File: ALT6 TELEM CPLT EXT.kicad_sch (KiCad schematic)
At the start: 22 parts, among them IC1 USBLC6-2SC6, IC2 USBLC6-2SC6, IC3 USBLC6-2SC6, J1 2200301031, J2 2200301031, J3 2200301021, J4 SSQ-120-01-L-D, J5 2200301031

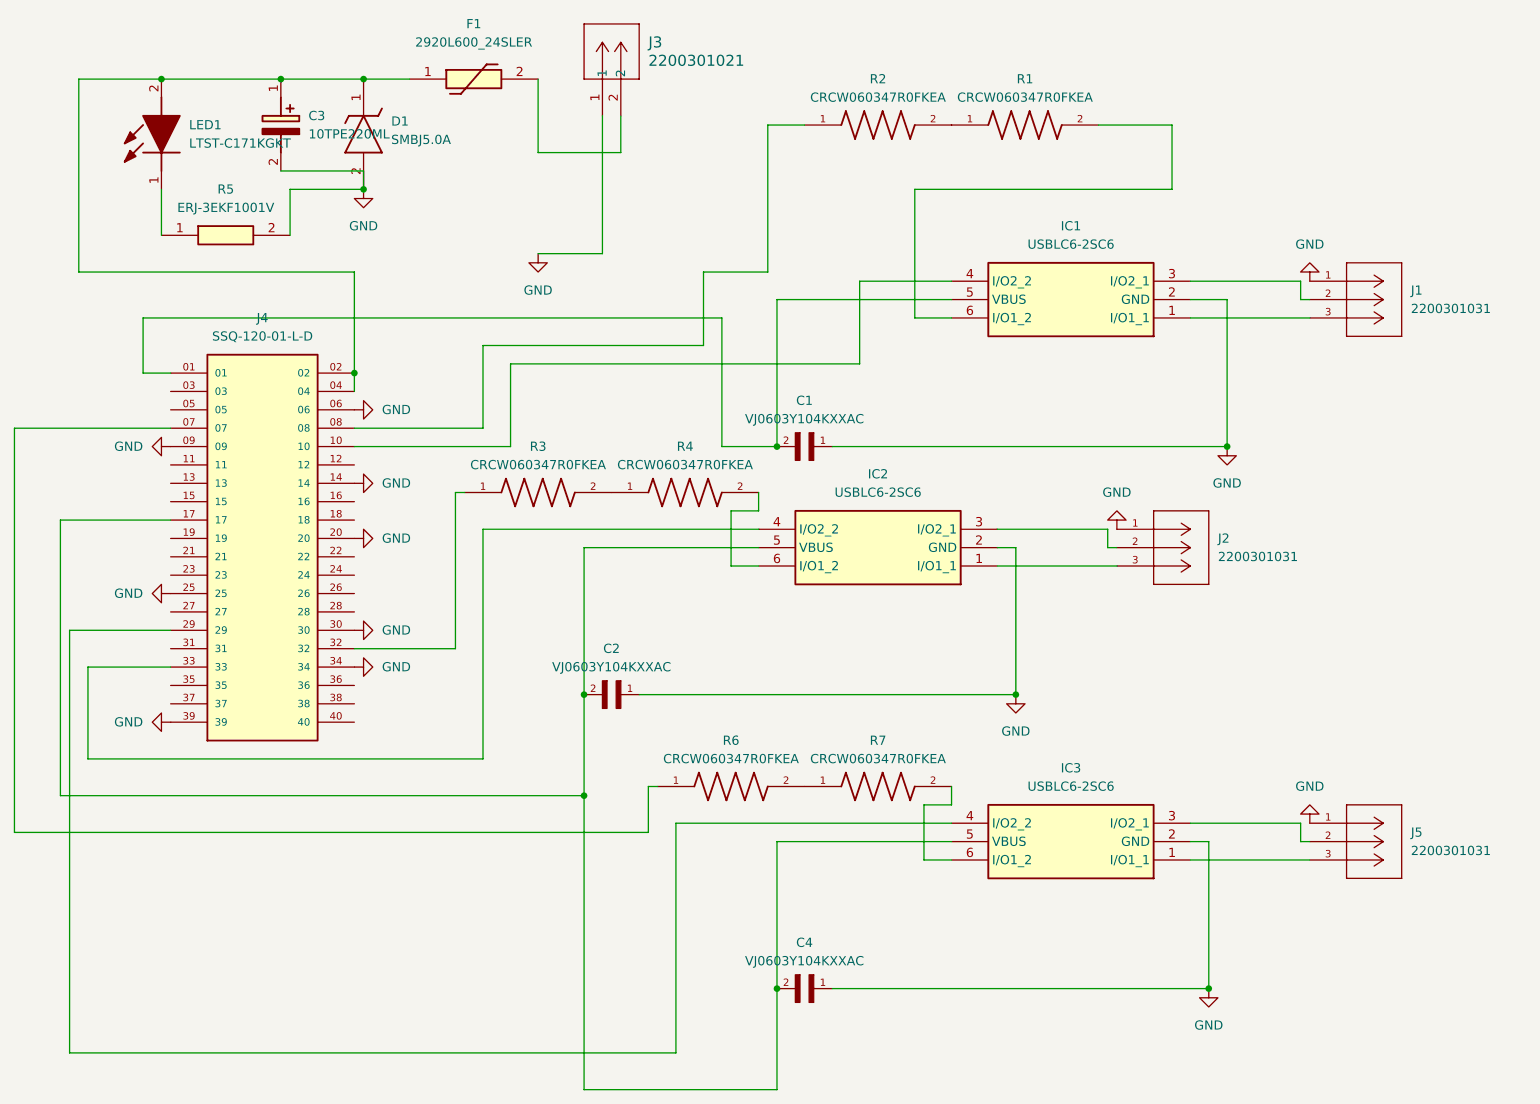
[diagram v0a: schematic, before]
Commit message: Connectors change
Connectors change to vertical, improve trace design, add 0ohm in RX line to test, change the power connector (was very big and innecesary)
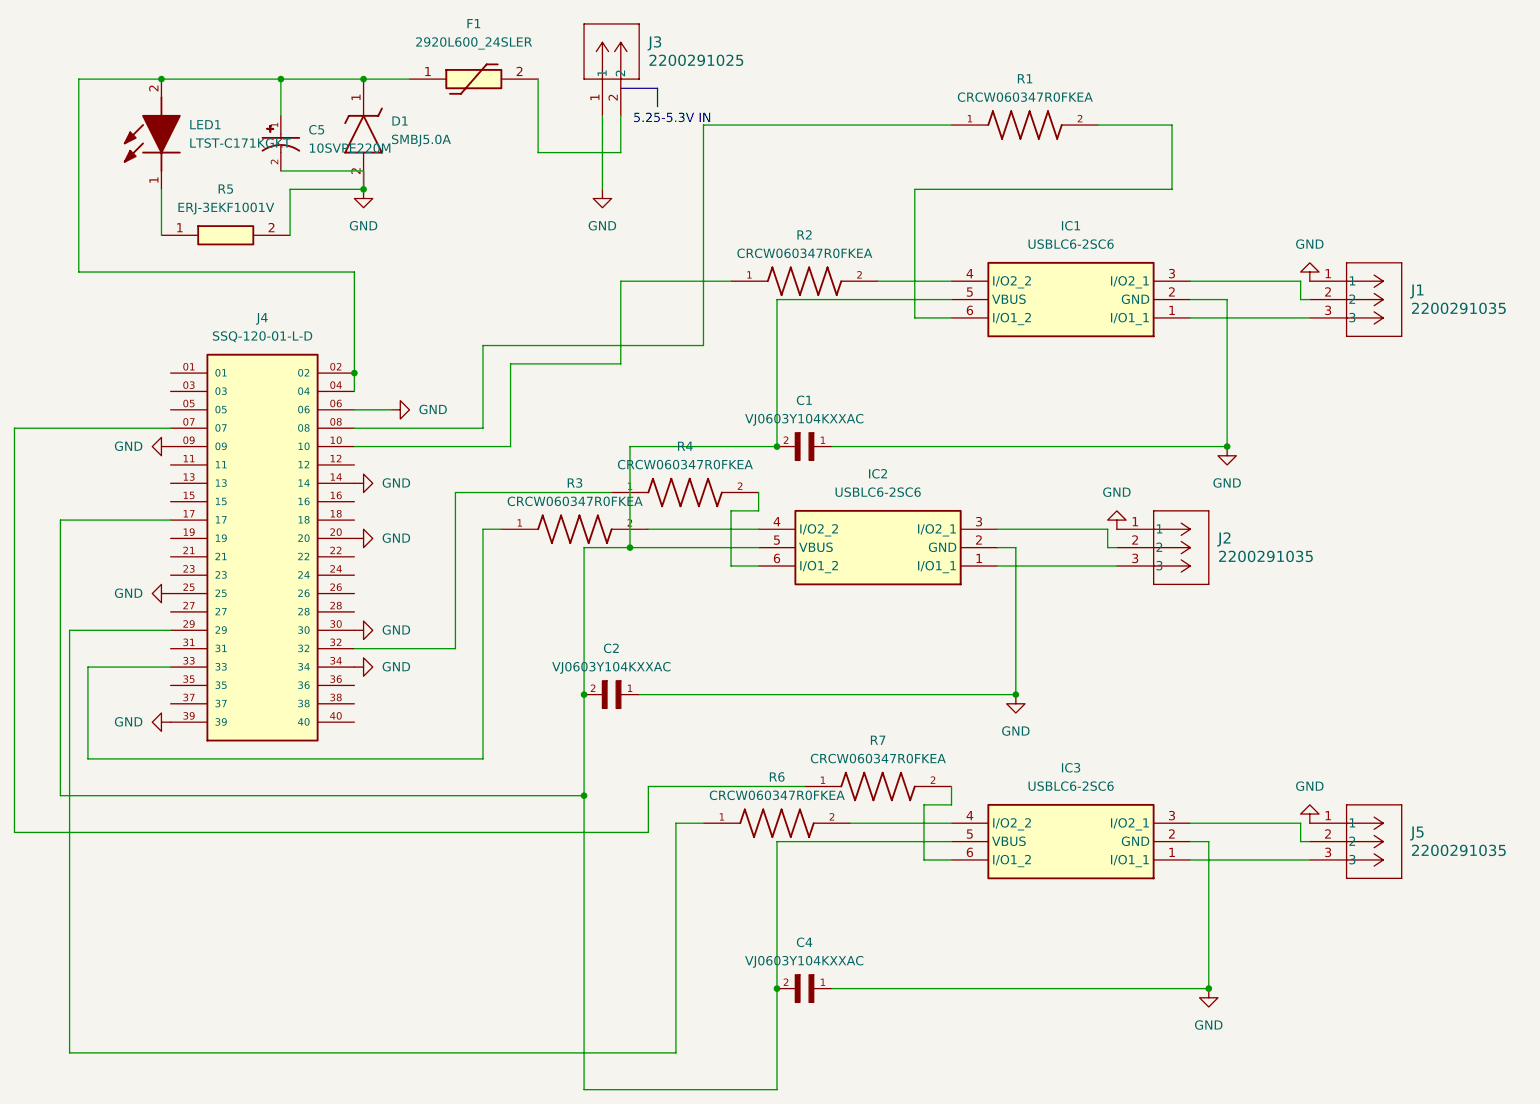
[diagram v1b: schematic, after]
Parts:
- removed C3: 10TPE220ML, 16TDC150MYF, symbol 10TPE220ML:10TPE220ML
- removed J1, J2, J5: 2200301031, 2200301031:CONN_2200300000-SD_03_MOL, symbol 2200301031:2200301031
- removed J3: 2200301021, CONN_2200300000-SD_02_MOL, symbol 2200301021:2200301021
- added C5: 10SVPE220M, 10SVPE220M:CAP_10SVPE220M, symbol 10SVPE220M:10SVPE220M
- added J1, J2, J5: 2200291035, CONN_2200290000-SD_03_MOL, symbol 2200291035:2200291035
- added J3: 2200291025, CONN_2200290000-SD_02_MOL, symbol 2200291025:2200291025
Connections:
- net GND: now also C5.2, J1.1, J2.1, J3.1, J5.1
- net at F1.2: now also J3.2
- net at C1.2, IC1.5 (VBUS): now also C2.2, C4.2, IC2.5 (VBUS), IC3.5 (VBUS), J4.17; no longer J4.01
- net at D1.1 (K), F1.1, J4.02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: now also C5.1
- net at J4.07: now also R7.1; no longer R6.1
- net at J4.08: now also R1.1; no longer R2.1
- net at J4.10: now also R2.1; no longer IC1.4 (I/O2_2)
- net at J4.29: now also R6.1; no longer IC3.4 (I/O2_2)
- net at J4.32: now also R4.1; no longer R3.1
- net at J4.33: now also R3.1; no longer IC2.4 (I/O2_2)
- net at R2.2: now also IC1.4 (I/O2_2); no longer R1.1
- net at IC3.1 (I/O1_1): now also J5.3
- net at IC3.3 (I/O2_1): now also J5.2
- net at R3.2: now also IC2.4 (I/O2_2); no longer R4.1
- net at IC1.1 (I/O1_1): now also J1.3
- net at IC1.3 (I/O2_1): now also J1.2
- net at R6.2: now also IC3.4 (I/O2_2); no longer R7.1
- net at IC2.3 (I/O2_1): now also J2.2
- net at IC2.1 (I/O1_1): now also J2.3
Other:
- note added: "5.25-5.3V IN"

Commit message: Complete Schematic
added labels in the schematic
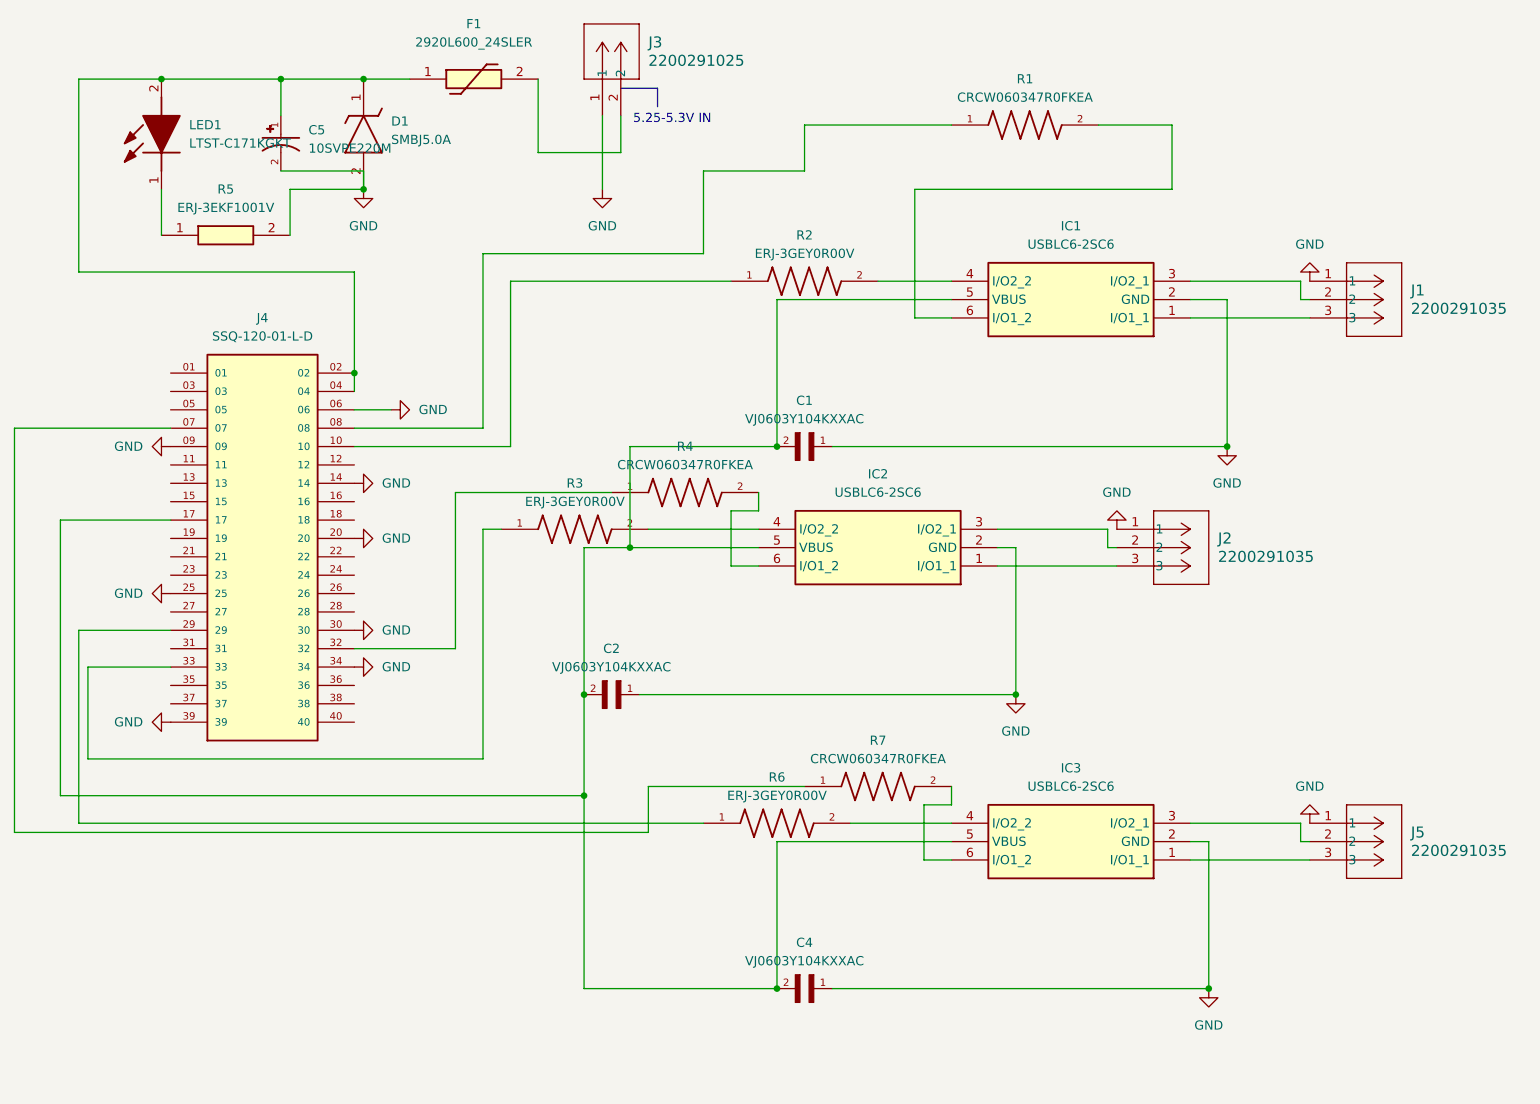
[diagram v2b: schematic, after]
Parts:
- removed R2, R3, R6: CRCW060347R0FKEA, CRCW060347R0FKEA:RESC1508X50N, symbol CRCW060347R0FKEA:CRCW060347R0FKEA
- added R2, R3, R6: ERJ-3GEY0R00V, ERJ-3GEY0R00V:RES_ERJ-3GEY0R00V, symbol ERJ-3GEY0R00V:ERJ-3GEY0R00V
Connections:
- net at J4.10: now also R2.1
- net at J4.29: now also R6.1
- net at J4.33: now also R3.1
- net at IC2.4 (I/O2_2): now also R3.2
- net at IC3.4 (I/O2_2): now also R6.2
- net at IC1.4 (I/O2_2): now also R2.2

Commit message: Reupload footprints
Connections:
- no-connect marks 0 -> 23
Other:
- note added: "PI5 40Pins Header"
- note added: "UART 0"
- note added: "UART 3"
- note added: "UART 5"
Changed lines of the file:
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@@
 	(generator_version "9.0")
 	(paper "A4")
+	(text "PI5 40Pins Header"
+		(exclude_from_sim no)
+		(at 84.328 59.182 0)
+		(effects
+			(font
+				(size 1.27 1.27)
+			)
+		)
+	)
+	(text "UART 0"
+		(exclude_from_sim no)
+		(at 268.732 65.278 0)
+		(effects
+			(font
+				(size 1.27 1.27)
+			)
+		)
+	)
 	(text "5.25-5.3V IN"
 		(exclude_from_sim no)
@@
 		)
 	)
+	(text "UART 5"
+		(exclude_from_sim no)
+		(at 268.732 140.208 0)
+		(effects
+			(font
+				(size 1.27 1.27)
+			)
+		)
+	)
+	(text "UART 3"
+		(exclude_from_sim no)
+		(at 242.062 99.568 0)
+		(effects
+			(font
+				(size 1.27 1.27)
+			)
+		)
+	)
 	(junction
 		(at 175.26 77.47)
@@
 		(color 0 0 0 0)
 	)
+	(no_connect
+		(at 91.44 85.09)
+	)
+	(no_connect
+		(at 91.44 105.41)
+	)
+	(no_connect
+		(at 91.44 113.03)
+	)
+	(no_connect
+		(at 116.84 113.03)
+	)
+	(no_connect
+		(at 91.44 67.31)
+	)
+	(no_connect
+		(at 91.44 90.17)
+	)
+	(no_connect
+		(at 116.84 87.63)
+	)
+	(no_connect
+		(at 91.44 110.49)
+	)
+	(no_connect
+		(at 116.84 95.25)
+	)
+	(no_connect
+		(at 116.84 92.71)
+	)
+	(no_connect
+		(at 116.84 85.09)
+	)
+	(no_connect
+		(at 91.44 80.01)
+	)
+	(no_connect
+		(at 91.44 100.33)
+	)
+	(no_connect
+		(at 91.44 69.85)
+	)
+	(no_connect
+		(at 91.44 82.55)
+	)
+	(no_connect
+		(at 116.84 110.49)
+	)
+	(no_connect
+		(at 116.84 80.01)
+	)
+	(no_connect
+		(at 91.44 92.71)
+	)
+	(no_connect
+		(at 91.44 95.25)
+	)
+	(no_connect
+		(at 116.84 97.79)
+	)
+	(no_connect
+		(at 116.84 115.57)
+	)
+	(no_connect
+		(at 116.84 100.33)
+	)
+	(no_connect
+		(at 91.44 72.39)
+	)
 	(wire
 		(pts
@@
 		)
 	)
+	(polyline
+		(pts
+			(xy 261.62 135.89) (xy 266.7 135.89)
+		)
+		(stroke
+			(width 0)
+			(type default)
+		)
+	)
 	(wire
 		(pts
@@
 		)
 	)
+	(polyline
+		(pts
+			(xy 240.03 95.25) (xy 240.03 97.79)
+		)
+		(stroke
+			(width 0)
+			(type default)
+		)
+	)
 	(wire
 		(pts
@@
 		)
 	)
+	(polyline
+		(pts
+			(xy 86.36 63.5) (xy 86.36 60.96)
+		)
+		(stroke
+			(width 0)
+			(type default)
+		)
+	)
 	(wire
 		(pts
@@
 		)
 	)
+	(polyline
+		(pts
+			(xy 261.62 60.96) (xy 266.7 60.96)
+		)
+		(stroke
+			(width 0)
+			(type default)
+		)
+	)
 	(wire
 		(pts
@@
 		)
 	)
+	(polyline
+		(pts
+			(xy 266.7 60.96) (xy 266.7 63.5)
+		)
+		(stroke
+			(width 0)
+			(type default)
+		)
+	)
+	(polyline
+		(pts
+			(xy 266.7 135.89) (xy 266.7 138.43)
+		)
+		(stroke
+			(width 0)
+			(type default)
+		)
+	)
 	(wire
 		(pts
@@
 		)
 	)
+	(polyline
+		(pts
+			(xy 96.52 64.77) (xy 86.36 63.5)
+		)
+		(stroke
+			(width 0)
+			(type default)
+		)
+	)
 	(wire
 		(pts
@@
 		)
 		(stroke
+			(width 0)
+			(type default)
+		)
+	)
+	(polyline
+		(pts
+			(xy 234.95 95.25) (xy 240.03 95.25)
+		)
+		(stroke
